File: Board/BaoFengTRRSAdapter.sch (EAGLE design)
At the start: 9 parts

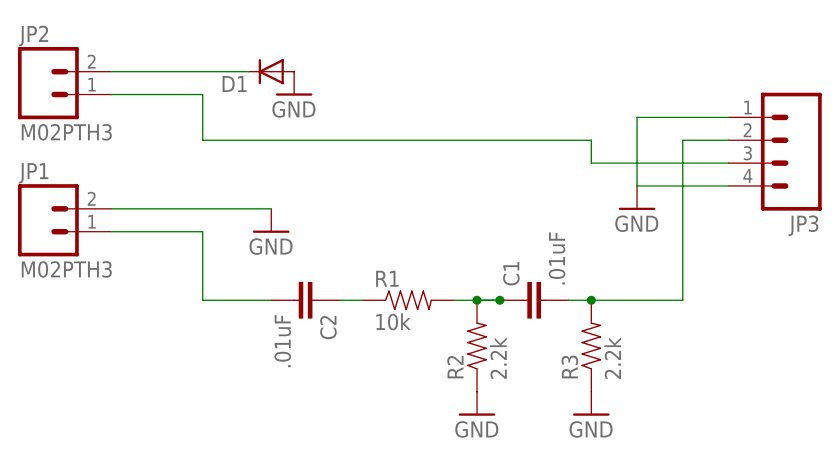
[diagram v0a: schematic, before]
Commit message: Removing unnecessary diode, making board a bit smaller
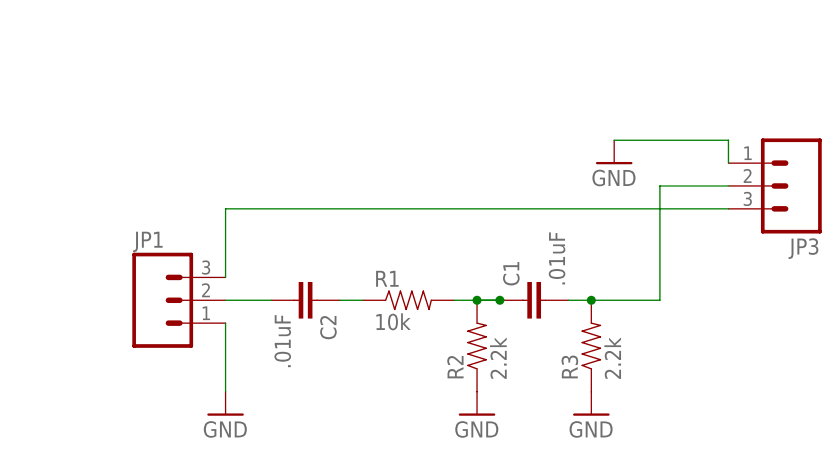
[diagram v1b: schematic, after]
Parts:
- removed D1: (no value), SparkFun-DiscreteSemi:DIODESMB
- removed JP2: M02PTH3, SparkFun-Connectors:M02PTH3
- JP1: value M02PTH3 -> (none); device SparkFun-Connectors:M02PTH3 -> SparkFun-Connectors:M031X03_NO_SILK
- JP3: device SparkFun-Connectors:M04LONGPADS -> SparkFun-Connectors:M031X03_NO_SILK
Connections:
- removed net BAOFENGMIC-: D1.C, JP2.2
- removed net BAOFENGSPK+: C2.2, JP1.1
- new net N$1: C2.2, JP1.2
- net BAOFENGMIC+: now also JP1.3; no longer JP2.1
- net GND: now also JP1.1; no longer D1.A, JP1.2, JP3.4
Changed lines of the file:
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@@
 </classes>
 <parts>
-<part name="D1" library="SparkFun-DiscreteSemi" deviceset="DIODE" device="SMB"/>
-<part name="GND1" library="SparkFun-Aesthetics" deviceset="GND" device=""/>
 <part name="GND2" library="SparkFun-Aesthetics" deviceset="GND" device=""/>
 <part name="R1" library="SparkFun-Passives" deviceset="RESISTOR" device="0603-RES" value="10k"/>
@@
 <part name="C2" library="SparkFun-Passives" deviceset="CAP" device="0603-CAP" value=".01uF"/>
 <part name="GND3" library="SparkFun-Aesthetics" deviceset="GND" device=""/>
-<part name="JP1" library="SparkFun-Connectors" deviceset="M02" device="PTH3"/>
-<part name="JP2" library="SparkFun-Connectors" deviceset="M02" device="PTH3"/>
-<part name="JP3" library="SparkFun-Connectors" deviceset="M04" device="LONGPADS"/>
+<part name="JP3" library="SparkFun-Connectors" deviceset="M03" device="1X03_NO_SILK"/>
+<part name="JP1" library="SparkFun-Connectors" deviceset="M03" device="1X03_NO_SILK"/>
 </parts>
 <sheets>
@@
 </plain>
 <instances>
-<instance part="D1" gate="G$1" x="63.5" y="96.52" rot="R180"/>
-<instance part="GND1" gate="1" x="66.04" y="93.98"/>
-<instance part="GND2" gate="1" x="63.5" y="78.74"/>
+<instance part="GND2" gate="1" x="58.42" y="58.42"/>
 <instance part="R1" gate="G$1" x="78.74" y="71.12"/>
 <instance part="R2" gate="G$1" x="86.36" y="66.04" rot="R90"/>
@@
 <instance part="GND5" gate="1" x="86.36" y="58.42"/>
 <instance part="C2" gate="G$1" x="66.04" y="71.12" rot="R270"/>
-<instance part="GND3" gate="1" x="104.14" y="81.28"/>
-<instance part="JP1" gate="G$1" x="38.1" y="78.74"/>
-<instance part="JP2" gate="G$1" x="38.1" y="93.98"/>
-<instance part="JP3" gate="G$1" x="119.38" y="88.9" rot="R180"/>
+<instance part="GND3" gate="1" x="101.6" y="86.36"/>
+<instance part="JP3" gate="G$1" x="121.92" y="83.82" rot="R180"/>
+<instance part="JP1" gate="G$1" x="50.8" y="71.12"/>
 </instances>
 <busses>
 </busses>
 <nets>
-<net name="BAOFENGMIC-" class="0">
-<segment>
-<pinref part="D1" gate="G$1" pin="C"/>
-<wire x1="60.96" y1="96.52" x2="45.72" y2="96.52" width="0.1524" layer="91"/>
-<pinref part="JP2" gate="G$1" pin="2"/>
-</segment>
-</net>
 <net name="GND" class="0">
-<segment>
-<pinref part="D1" gate="G$1" pin="A"/>
-<pinref part="GND1" gate="1" pin="GND"/>
-</segment>
-<segment>
-<pinref part="GND2" gate="1" pin="GND"/>
-<wire x1="45.72" y1="81.28" x2="63.5" y2="81.28" width="0.1524" layer="91"/>
-<pinref part="JP1" gate="G$1" pin="2"/>
-</segment>
 <segment>
 <pinref part="R3" gate="G$1" pin="1"/>
@@
 </segment>
 <segment>
-<wire x1="114.3" y1="91.44" x2="104.14" y2="91.44" width="0.1524" layer="91"/>
 <pinref part="GND3" gate="1" pin="GND"/>
-<wire x1="104.14" y1="91.44" x2="104.14" y2="83.82" width="0.1524" layer="91"/>
+<wire x1="101.6" y1="88.9" x2="114.3" y2="88.9" width="0.1524" layer="91"/>
 <pinref part="JP3" gate="G$1" pin="1"/>
-<pinref part="JP3" gate="G$1" pin="4"/>
-<wire x1="114.3" y1="83.82" x2="104.14" y2="83.82" width="0.1524" layer="91"/>
+<wire x1="114.3" y1="88.9" x2="114.3" y2="86.36" width="0.1524" layer="91"/>
+</segment>
+<segment>
+<pinref part="JP1" gate="G$1" pin="1"/>
+<pinref part="GND2" gate="1" pin="GND"/>
+<wire x1="58.42" y1="60.96" x2="58.42" y2="68.58" width="0.1524" layer="91"/>
 </segment>
 </net>
 <net name="BAOFENGMIC+" class="0">
 <segment>
-<wire x1="45.72" y1="93.98" x2="55.88" y2="93.98" width="0.1524" layer="91"/>
-<wire x1="55.88" y1="93.98" x2="55.88" y2="88.9" width="0.1524" layer="91"/>
-<pinref part="JP2" gate="G$1" pin="1"/>
-<wire x1="55.88" y1="88.9" x2="99.06" y2="88.9" width="0.1524" layer="91"/>
-<wire x1="99.06" y1="88.9" x2="99.06" y2="86.36" width="0.1524" layer="91"/>
-<wire x1="99.06" y1="86.36" x2="114.3" y2="86.36" width="0.1524" layer="91"/>
+<wire x1="58.42" y1="81.28" x2="114.3" y2="81.28" width="0.1524" layer="91"/>
 <pinref part="JP3" gate="G$1" pin="3"/>
+<pinref part="JP1" gate="G$1" pin="3"/>
+<wire x1="58.42" y1="81.28" x2="58.42" y2="73.66" width="0.1524" layer="91"/>
 </segment>
 </net>
@@
 <pinref part="R3" gate="G$1" pin="2"/>
 <wire x1="96.52" y1="71.12" x2="99.06" y2="71.12" width="0.1524" layer="91"/>
-<wire x1="99.06" y1="71.12" x2="109.22" y2="71.12" width="0.1524" layer="91"/>
-<wire x1="109.22" y1="71.12" x2="109.22" y2="88.9" width="0.1524" layer="91"/>
-<wire x1="109.22" y1="88.9" x2="114.3" y2="88.9" width="0.1524" layer="91"/>
+<wire x1="99.06" y1="71.12" x2="106.68" y2="71.12" width="0.1524" layer="91"/>
+<wire x1="106.68" y1="71.12" x2="106.68" y2="83.82" width="0.1524" layer="91"/>
+<wire x1="106.68" y1="83.82" x2="114.3" y2="83.82" width="0.1524" layer="91"/>
+<junction x="99.06" y="71.12"/>
 <pinref part="JP3" gate="G$1" pin="2"/>
-<junction x="99.06" y="71.12"/>
-</segment>
-</net>
-<net name="BAOFENGSPK+" class="0">
-<segment>
-<wire x1="45.72" y1="78.74" x2="55.88" y2="78.74" width="0.1524" layer="91"/>
-<wire x1="55.88" y1="78.74" x2="55.88" y2="71.12" width="0.1524" layer="91"/>
-<pinref part="C2" gate="G$1" pin="2"/>
-<wire x1="55.88" y1="71.12" x2="63.5" y2="71.12" width="0.1524" layer="91"/>
-<pinref part="JP1" gate="G$1" pin="1"/>
 </segment>
 </net>
@@
 </segment>
 </net>
+<net name="N$1" class="0">
+<segment>
+<pinref part="JP1" gate="G$1" pin="2"/>
+<pinref part="C2" gate="G$1" pin="2"/>
+<wire x1="58.42" y1="71.12" x2="63.5" y2="71.12" width="0.1524" layer="91"/>
+</segment>
+</net>
 </nets>
 </sheet>
 </sheets>
+<errors>
+</errors>
 </schematic>
 </drawing>

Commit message: update to improve detection on various phones (#19)
Co-authored-by: kronicd <aaa>
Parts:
- added R4: 0.1k, SparkFun-Passives:RESISTOR0603-RES
- R3: SPICEPREFIX (none) -> R
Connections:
- net BAOFENGMIC+: now also R4.2
- net GND: now also R4.1
